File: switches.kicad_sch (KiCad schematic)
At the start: 18 parts, among them SW1 DS04-254-1L-08BK, SW2 DS04-254-1L-08BK

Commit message: Schematic is done?
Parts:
- R57, R58, R59, R60, R61, R62, R63, R64, R66, R67, R68, R69, R70, R71, R72, R73: footprint (none) -> Resistor_SMD:R_0402_1005Metric; symbol Device:R_US -> CMPE2750:0402WGJ0103TCE
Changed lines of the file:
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@@
 	)
 	(symbol
-		(lib_id "Device:R_US")
+		(lib_id "CMPE2750:0402WGJ0103TCE")
 		(at 22.86 129.54 0)
 		(unit 1)
@@
 			)
 		)
-		(property "Footprint" ""
+		(property "Footprint" "Resistor_SMD:R_0402_1005Metric"
 			(at 23.876 129.794 90)
 			(effects
@@
 			)
 		)
-		(property "Datasheet" "~"
+		(property "Datasheet" "0402WGJ0103TCE"
 			(at 22.86 129.54 0)
 			(effects
@@
 	)
 	(symbol
-		(lib_id "Device:R_US")
+		(lib_id "CMPE2750:0402WGJ0103TCE")
 		(at 46.99 33.02 0)
 		(unit 1)
@@
 			)
 		)
-		(property "Footprint" ""
+		(property "Footprint" "Resistor_SMD:R_0402_1005Metric"
 			(at 48.006 33.274 90)
 			(effects
@@
 			)
 		)
-		(property "Datasheet" "~"
+		(property "Datasheet" "0402WGJ0103TCE"
 			(at 46.99 33.02 0)
 			(effects
@@
 	)
 	(symbol
-		(lib_id "Device:R_US")
+		(lib_id "CMPE2750:0402WGJ0103TCE")
 		(at 46.99 92.71 0)
 		(unit 1)
@@
 			)
 		)
-		(property "Footprint" ""
+		(property "Footprint" "Resistor_SMD:R_0402_1005Metric"
 			(at 48.006 92.964 90)
 			(effects
@@
 			)
 		)
-		(property "Datasheet" "~"
+		(property "Datasheet" "0402WGJ0103TCE"
 			(at 46.99 92.71 0)
 			(effects
@@
 	)
 	(symbol
-		(lib_id "Device:R_US")
+		(lib_id "CMPE2750:0402WGJ0103TCE")
 		(at 22.86 72.39 0)
 		(unit 1)
@@
 			)
 		)
-		(property "Footprint" ""
+		(property "Footprint" "Resistor_SMD:R_0402_1005Metric"
 			(at 23.876 72.644 90)
 			(effects
@@
 			)
 		)
-		(property "Datasheet" "~"
+		(property "Datasheet" "0402WGJ0103TCE"
 			(at 22.86 72.39 0)
 			(effects
@@
 	)
 	(symbol
-		(lib_id "Device:R_US")
+		(lib_id "CMPE2750:0402WGJ0103TCE")
 		(at 46.99 72.39 0)
 		(unit 1)
@@
 			)
 		)
-		(property "Footprint" ""
+		(property "Footprint" "Resistor_SMD:R_0402_1005Metric"
 			(at 48.006 72.644 90)
 			(effects
@@
 			)
 		)
-		(property "Datasheet" "~"
+		(property "Datasheet" "0402WGJ0103TCE"
 			(at 46.99 72.39 0)
 			(effects
@@
 	)
 	(symbol
-		(lib_id "Device:R_US")
+		(lib_id "CMPE2750:0402WGJ0103TCE")
 		(at 46.99 110.49 0)
 		(unit 1)
@@
 			)
 		)
-		(property "Footprint" ""
+		(property "Footprint" "Resistor_SMD:R_0402_1005Metric"
 			(at 48.006 110.744 90)
 			(effects
@@
 			)
 		)
-		(property "Datasheet" "~"
+		(property "Datasheet" "0402WGJ0103TCE"
 			(at 46.99 110.49 0)
 			(effects
@@
 	)
 	(symbol
-		(lib_id "Device:R_US")
+		(lib_id "CMPE2750:0402WGJ0103TCE")
 		(at 22.86 34.29 0)
 		(unit 1)
@@
 			)
 		)
-		(property "Footprint" ""
+		(property "Footprint" "Resistor_SMD:R_0402_1005Metric"
 			(at 23.876 34.544 90)
 			(effects
@@
 			)
 		)
-		(property "Datasheet" "~"
+		(property "Datasheet" "0402WGJ0103TCE"
 			(at 22.86 34.29 0)
 			(effects
@@
 	)
 	(symbol
-		(lib_id "Device:R_US")
+		(lib_id "CMPE2750:0402WGJ0103TCE")
 		(at 46.99 128.27 0)
 		(unit 1)
@@
 			)
 		)
-		(property "Footprint" ""
+		(property "Footprint" "Resistor_SMD:R_0402_1005Metric"
 			(at 48.006 128.524 90)
 			(effects
@@
 			)
 		)
-		(property "Datasheet" "~"
+		(property "Datasheet" "0402WGJ0103TCE"
 			(at 46.99 128.27 0)
 			(effects
@@
 	)
 	(symbol
-		(lib_id "Device:R_US")
+		(lib_id "CMPE2750:0402WGJ0103TCE")
 		(at 22.86 147.32 0)
 		(unit 1)
@@
 			)
 		)
-		(property "Footprint" ""
+		(property "Footprint" "Resistor_SMD:R_0402_1005Metric"
 			(at 23.876 147.574 90)
 			(effects
@@
 			)
 		)
-		(property "Datasheet" "~"
+		(property "Datasheet" "0402WGJ0103TCE"
 			(at 22.86 147.32 0)
 			(effects
@@
 	)
 	(symbol
-		(lib_id "Device:R_US")
+		(lib_id "CMPE2750:0402WGJ0103TCE")
 		(at 48.26 167.64 0)
 		(unit 1)
@@
 			)
 		)
-		(property "Footprint" ""
+		(property "Footprint" "Resistor_SMD:R_0402_1005Metric"
 			(at 49.276 167.894 90)
 			(effects
@@
 			)
 		)
-		(property "Datasheet" "~"
+		(property "Datasheet" "0402WGJ0103TCE"
 			(at 48.26 167.64 0)
 			(effects
@@
 	)
 	(symbol
-		(lib_id "Device:R_US")
+		(lib_id "CMPE2750:0402WGJ0103TCE")
 		(at 22.86 111.76 0)
 		(unit 1)
@@
 			)
 		)
-		(property "Footprint" ""
+		(property "Footprint" "Resistor_SMD:R_0402_1005Metric"
 			(at 23.876 112.014 90)
 			(effects
@@
 			)
 		)
-		(property "Datasheet" "~"
+		(property "Datasheet" "0402WGJ0103TCE"
 			(at 22.86 111.76 0)
 			(effects
@@
 	)
 	(symbol
-		(lib_id "Device:R_US")
+		(lib_id "CMPE2750:0402WGJ0103TCE")
 		(at 22.86 53.34 0)
 		(unit 1)
@@
 			)
 		)
-		(property "Footprint" ""
+		(property "Footprint" "Resistor_SMD:R_0402_1005Metric"
 			(at 23.876 53.594 90)
 			(effects
@@
 			)
 		)
-		(property "Datasheet" "~"
+		(property "Datasheet" "0402WGJ0103TCE"
 			(at 22.86 53.34 0)
 			(effects
@@
 	)
 	(symbol
-		(lib_id "Device:R_US")
+		(lib_id "CMPE2750:0402WGJ0103TCE")
 		(at 22.86 93.98 0)
 		(unit 1)
@@
 			)
 		)
-		(property "Footprint" ""
+		(property "Footprint" "Resistor_SMD:R_0402_1005Metric"
 			(at 23.876 94.234 90)
 			(effects
@@
 			)
 		)
-		(property "Datasheet" "~"
+		(property "Datasheet" "0402WGJ0103TCE"
 			(at 22.86 93.98 0)
 			(effects
@@
 	)
 	(symbol
-		(lib_id "Device:R_US")
+		(lib_id "CMPE2750:0402WGJ0103TCE")
 		(at 46.99 49.53 0)
 		(unit 1)
@@
 			)
 		)
-		(property "Footprint" ""
+		(property "Footprint" "Resistor_SMD:R_0402_1005Metric"
 			(at 48.006 49.784 90)
 			(effects
@@
 			)
 		)
-		(property "Datasheet" "~"
+		(property "Datasheet" "0402WGJ0103TCE"
 			(at 46.99 49.53 0)
 			(effects
@@
 	)
 	(symbol
-		(lib_id "Device:R_US")
+		(lib_id "CMPE2750:0402WGJ0103TCE")
 		(at 46.99 146.05 0)
 		(unit 1)
@@
 			)
 		)
-		(property "Footprint" ""
+		(property "Footprint" "Resistor_SMD:R_0402_1005Metric"
 			(at 48.006 146.304 90)
 			(effects
@@
 			)
 		)
-		(property "Datasheet" "~"
+		(property "Datasheet" "0402WGJ0103TCE"
 			(at 46.99 146.05 0)
 			(effects
@@
 	)
 	(symbol
-		(lib_id "Device:R_US")
+		(lib_id "CMPE2750:0402WGJ0103TCE")
 		(at 22.86 165.1 0)
 		(unit 1)
@@
 			)
 		)
-		(property "Footprint" ""
+		(property "Footprint" "Resistor_SMD:R_0402_1005Metric"
 			(at 23.876 165.354 90)
 			(effects
@@
 			)
 		)
-		(property "Datasheet" "~"
+		(property "Datasheet" "0402WGJ0103TCE"
 			(at 22.86 165.1 0)
 			(effects

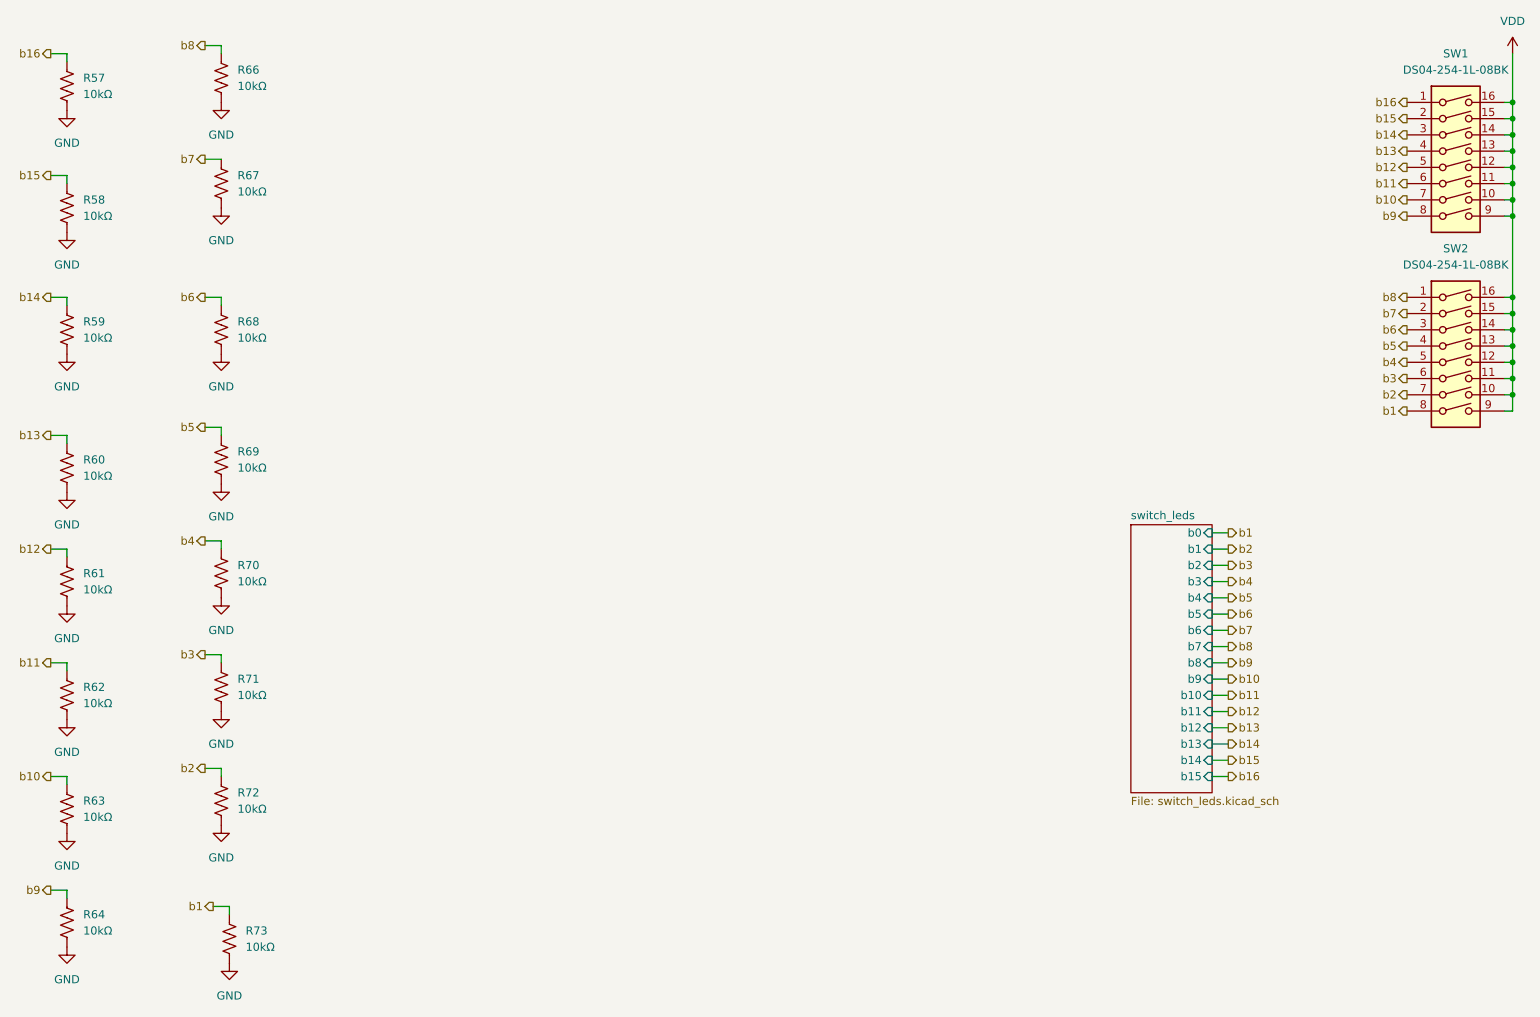
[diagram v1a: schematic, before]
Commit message: Added mounting holes to the schematic, reset the annotations, updated a few footprints, and fixed some issues that were discovered on the ERC.
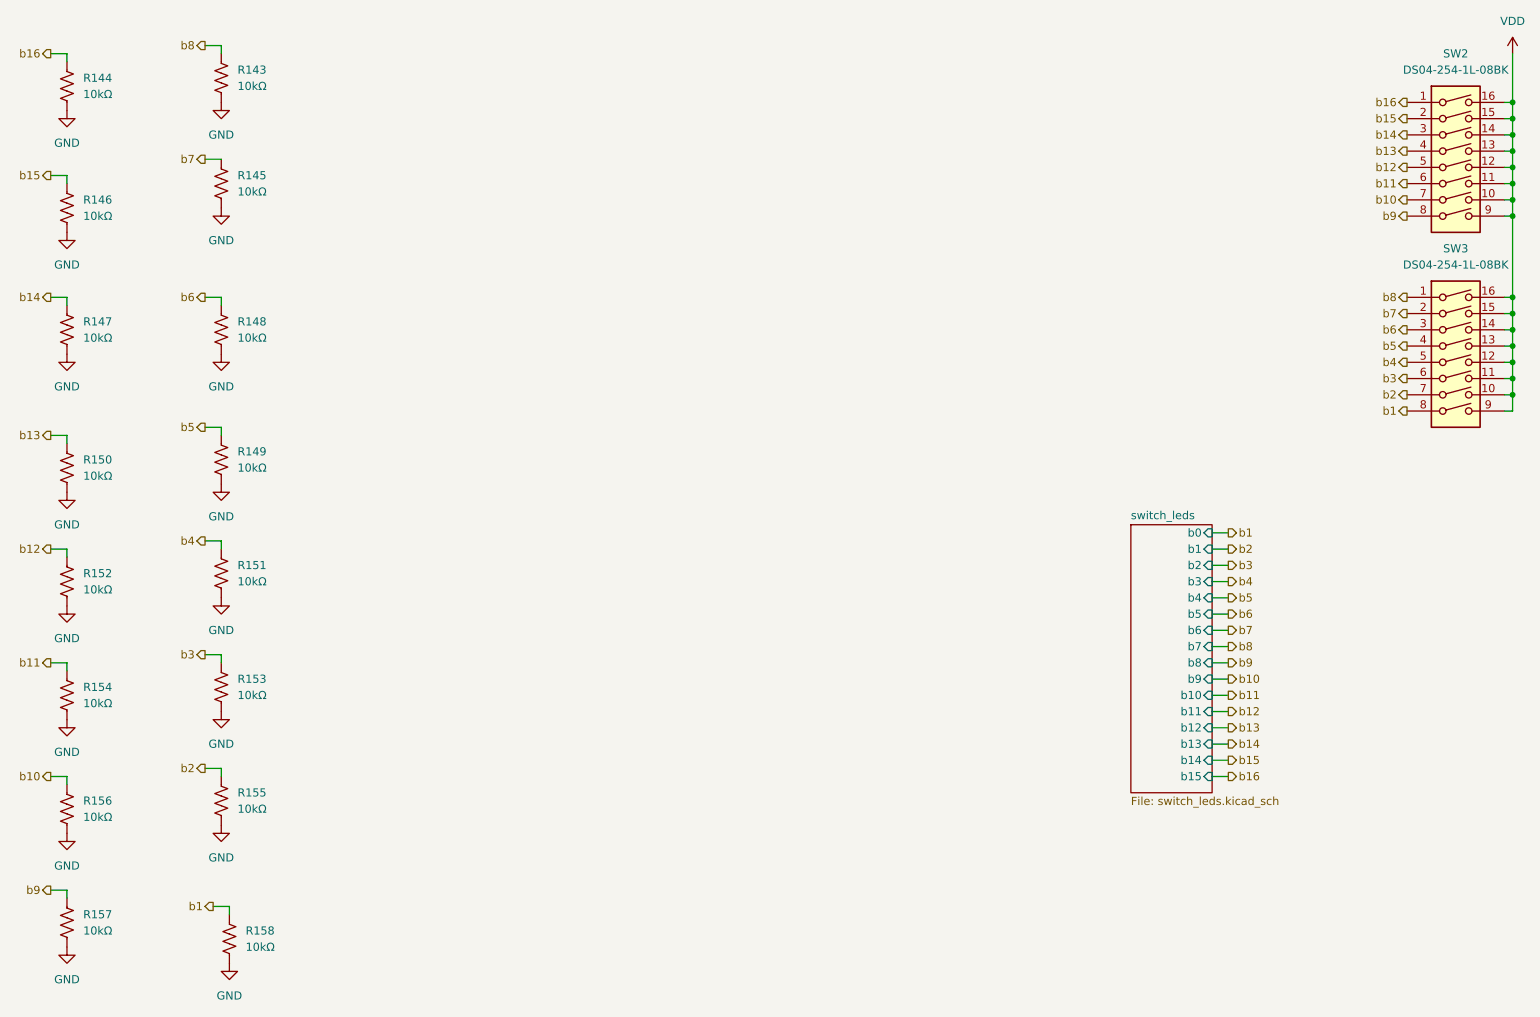
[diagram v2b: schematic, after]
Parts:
- renumbered R66 to R143, R57 to R144, R67 to R145, R58 to R146, R59 to R147, R68 to R148, R69 to R149, R60 to R150, R70 to R151, R61 to R152, R71 to R153, R62 to R154, R72 to R155, R63 to R156, R64 to R157, R73 to R158, SW1 to SW2, SW2 to SW3
